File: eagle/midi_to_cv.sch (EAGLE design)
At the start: 75 parts, among them IC1 TL082P, IC2 TL084P, IC4 TL082P, IC6 TL082P, IC7 TL082P, U1 ATMEGA328P_PDIP, U2 MCP4822-E/P, U3 MCP4822-E/P, U4 MCP4822-E/P, U5 MCP4822-E/P

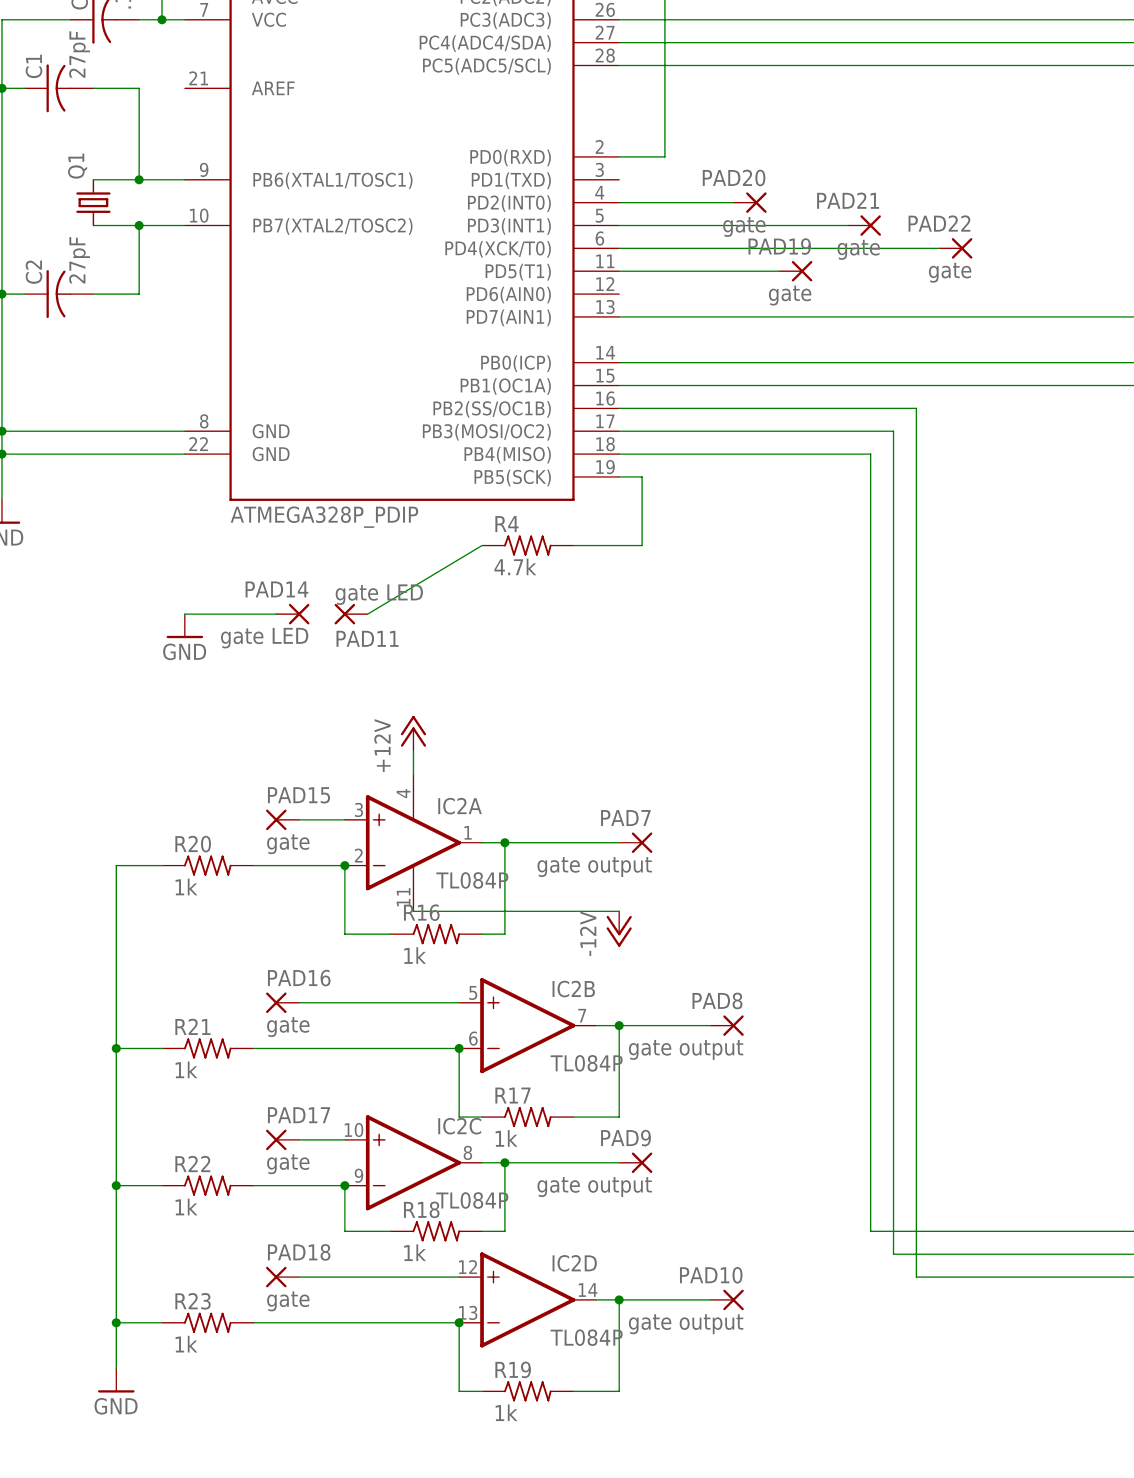
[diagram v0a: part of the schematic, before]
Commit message: will route gates to op amps instead of jumper pads
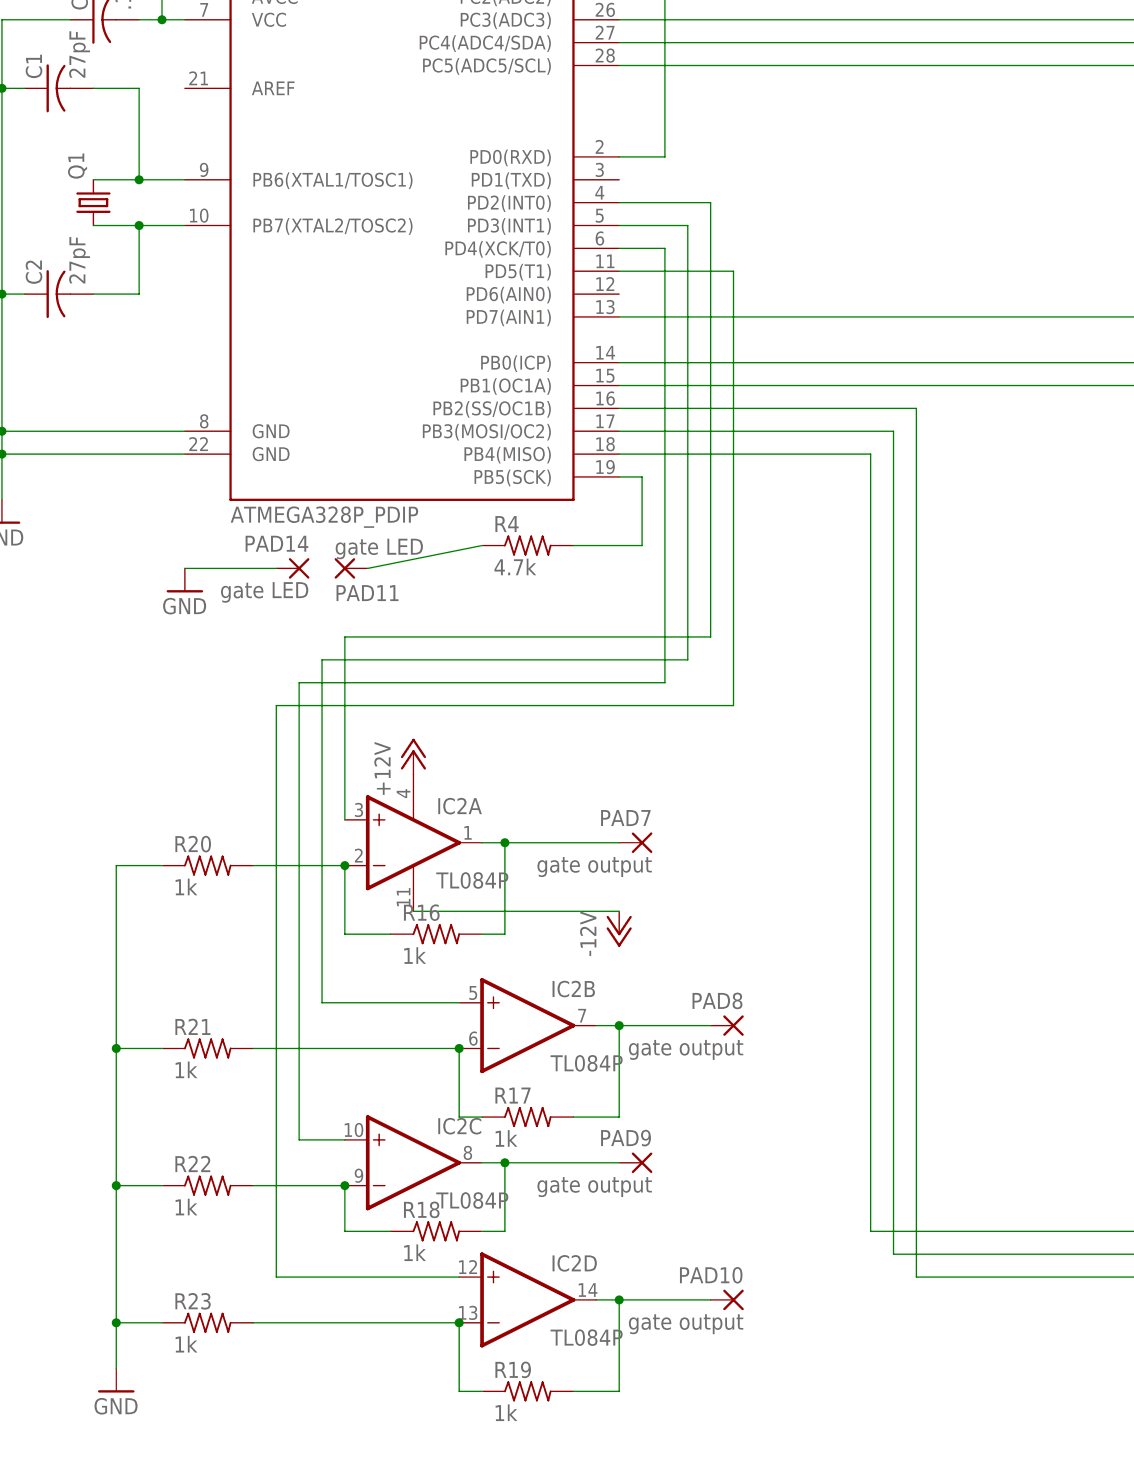
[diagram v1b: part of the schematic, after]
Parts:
- removed PAD15, PAD16, PAD17, PAD18, PAD19, PAD20, PAD21, PAD22: gate, wirepad:2,54/0,9
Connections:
- removed net N$31: PAD19.P, U1.PD5(T1)
- removed net N$32: PAD20.P, U1.PD2(INT0)
- removed net N$33: PAD21.P, U1.PD3(INT1)
- removed net N$43: PAD22.P, U1.PD4(XCK/T0)
- net N$34: now also U1.PD5(T1); no longer PAD18.P
- net N$44: now also U1.PD4(XCK/T0); no longer PAD17.P
- net N$45: now also U1.PD3(INT1); no longer PAD16.P
- net N$46: now also U1.PD2(INT0); no longer PAD15.P
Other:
- moved on the sheet: PAD11, PAD14
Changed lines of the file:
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@@
 <part name="P-2" library="supply1" deviceset="-12V" device=""/>
 <part name="P+8" library="supply1" deviceset="+12V" device=""/>
-<part name="PAD15" library="wirepad" deviceset="2,54/0,9" device="" value="gate"/>
-<part name="PAD16" library="wirepad" deviceset="2,54/0,9" device="" value="gate"/>
-<part name="PAD17" library="wirepad" deviceset="2,54/0,9" device="" value="gate"/>
-<part name="PAD18" library="wirepad" deviceset="2,54/0,9" device="" value="gate"/>
-<part name="PAD19" library="wirepad" deviceset="2,54/0,9" device="" value="gate"/>
-<part name="PAD20" library="wirepad" deviceset="2,54/0,9" device="" value="gate"/>
-<part name="PAD21" library="wirepad" deviceset="2,54/0,9" device="" value="gate"/>
-<part name="PAD22" library="wirepad" deviceset="2,54/0,9" device="" value="gate"/>
 <part name="GND5" library="supply1" deviceset="GND" device=""/>
 <part name="R8" library="rcl" deviceset="R-US_" device="0207/10" value="3.3k"/>
@@
 <instance part="IC2" gate="C" x="20.32" y="-60.96"/>
 <instance part="IC2" gate="D" x="33.02" y="-76.2"/>
-<instance part="PAD11" gate="1" x="12.7" y="0" rot="MR180"/>
+<instance part="PAD11" gate="1" x="12.7" y="5.08" rot="MR180"/>
 <instance part="R4" gate="G$1" x="33.02" y="7.62"/>
 <instance part="R16" gate="G$1" x="22.86" y="-35.56"/>
@@
 <instance part="PAD13" gate="1" x="10.16" y="83.82" rot="MR180"/>
 <instance part="GND9" gate="1" x="20.32" y="81.28"/>
-<instance part="PAD14" gate="1" x="7.62" y="0" rot="MR0"/>
-<instance part="GND11" gate="1" x="-5.08" y="-2.54"/>
+<instance part="PAD14" gate="1" x="7.62" y="5.08" rot="MR0"/>
+<instance part="GND11" gate="1" x="-5.08" y="2.54"/>
 <instance part="P-2" gate="1" x="43.18" y="-35.56"/>
-<instance part="P+8" gate="1" x="20.32" y="-12.7"/>
+<instance part="P+8" gate="1" x="20.32" y="-15.24"/>
 <instance part="IC2" gate="P" x="20.32" y="-25.4"/>
-<instance part="PAD15" gate="1" x="5.08" y="-22.86"/>
-<instance part="PAD16" gate="1" x="5.08" y="-43.18"/>
-<instance part="PAD17" gate="1" x="5.08" y="-58.42"/>
-<instance part="PAD18" gate="1" x="5.08" y="-73.66"/>
-<instance part="PAD19" gate="1" x="63.5" y="38.1" rot="MR0"/>
-<instance part="PAD20" gate="1" x="58.42" y="45.72" rot="MR0"/>
-<instance part="PAD21" gate="1" x="71.12" y="43.18" rot="MR0"/>
-<instance part="PAD22" gate="1" x="81.28" y="40.64" rot="MR0"/>
 <instance part="GND5" gate="1" x="109.22" y="-86.36"/>
 <instance part="R8" gate="G$1" x="177.8" y="124.46"/>
@@
 </segment>
 <segment>
-<wire x1="-5.08" y1="0" x2="5.08" y2="0" width="0.1524" layer="91"/>
+<wire x1="-5.08" y1="5.08" x2="5.08" y2="5.08" width="0.1524" layer="91"/>
 <pinref part="PAD14" gate="1" pin="P"/>
 <pinref part="GND11" gate="1" pin="GND"/>
@@
 <segment>
 <pinref part="P+8" gate="1" pin="+12V"/>
-<wire x1="20.32" y1="-17.78" x2="20.32" y2="-15.24" width="0.1524" layer="91"/>
 <pinref part="IC2" gate="P" pin="V+"/>
 </segment>
@@
 <pinref part="R4" gate="G$1" pin="1"/>
 <pinref part="PAD11" gate="1" pin="P"/>
-<wire x1="27.94" y1="7.62" x2="15.24" y2="0" width="0.1524" layer="91"/>
-</segment>
-</net>
-<net name="N$32" class="0">
-<segment>
-<pinref part="U1" gate="G$1" pin="PD2(INT0)"/>
-<wire x1="43.18" y1="45.72" x2="55.88" y2="45.72" width="0.1524" layer="91"/>
-<pinref part="PAD20" gate="1" pin="P"/>
-</segment>
-</net>
-<net name="N$33" class="0">
-<segment>
-<pinref part="U1" gate="G$1" pin="PD3(INT1)"/>
-<wire x1="43.18" y1="43.18" x2="68.58" y2="43.18" width="0.1524" layer="91"/>
-<pinref part="PAD21" gate="1" pin="P"/>
+<wire x1="27.94" y1="7.62" x2="15.24" y2="5.08" width="0.1524" layer="91"/>
 </segment>
 </net>
@@
 <segment>
 <pinref part="IC2" gate="D" pin="+IN"/>
-<wire x1="7.62" y1="-73.66" x2="25.4" y2="-73.66" width="0.1524" layer="91"/>
-<pinref part="PAD18" gate="1" pin="P"/>
+<wire x1="5.08" y1="-73.66" x2="25.4" y2="-73.66" width="0.1524" layer="91"/>
+<wire x1="5.08" y1="-73.66" x2="5.08" y2="-10.16" width="0.1524" layer="91"/>
+<wire x1="5.08" y1="-10.16" x2="55.88" y2="-10.16" width="0.1524" layer="91"/>
+<wire x1="55.88" y1="-10.16" x2="55.88" y2="38.1" width="0.1524" layer="91"/>
+<pinref part="U1" gate="G$1" pin="PD5(T1)"/>
+<wire x1="55.88" y1="38.1" x2="43.18" y2="38.1" width="0.1524" layer="91"/>
 </segment>
 </net>
@@
 </segment>
 </net>
-<net name="N$43" class="0">
-<segment>
-<pinref part="U1" gate="G$1" pin="PD4(XCK/T0)"/>
-<wire x1="43.18" y1="40.64" x2="78.74" y2="40.64" width="0.1524" layer="91"/>
-<pinref part="PAD22" gate="1" pin="P"/>
-</segment>
-</net>
 <net name="N$44" class="0">
 <segment>
 <pinref part="IC2" gate="C" pin="+IN"/>
 <wire x1="7.62" y1="-58.42" x2="12.7" y2="-58.42" width="0.1524" layer="91"/>
-<pinref part="PAD17" gate="1" pin="P"/>
+<pinref part="U1" gate="G$1" pin="PD4(XCK/T0)"/>
+<wire x1="43.18" y1="40.64" x2="48.26" y2="40.64" width="0.1524" layer="91"/>
+<wire x1="48.26" y1="40.64" x2="48.26" y2="-7.62" width="0.1524" layer="91"/>
+<wire x1="48.26" y1="-7.62" x2="7.62" y2="-7.62" width="0.1524" layer="91"/>
+<wire x1="7.62" y1="-7.62" x2="7.62" y2="-58.42" width="0.1524" layer="91"/>
 </segment>
 </net>
@@
 <segment>
 <pinref part="IC2" gate="B" pin="+IN"/>
-<wire x1="7.62" y1="-43.18" x2="25.4" y2="-43.18" width="0.1524" layer="91"/>
-<pinref part="PAD16" gate="1" pin="P"/>
+<pinref part="U1" gate="G$1" pin="PD3(INT1)"/>
+<wire x1="10.16" y1="-43.18" x2="25.4" y2="-43.18" width="0.1524" layer="91"/>
+<wire x1="43.18" y1="43.18" x2="50.8" y2="43.18" width="0.1524" layer="91"/>
+<wire x1="50.8" y1="43.18" x2="50.8" y2="-5.08" width="0.1524" layer="91"/>
+<wire x1="50.8" y1="-5.08" x2="10.16" y2="-5.08" width="0.1524" layer="91"/>
+<wire x1="10.16" y1="-5.08" x2="10.16" y2="-43.18" width="0.1524" layer="91"/>
 </segment>
 </net>
 <net name="N$46" class="0">
 <segment>
-<pinref part="PAD15" gate="1" pin="P"/>
 <pinref part="IC2" gate="A" pin="+IN"/>
-<wire x1="7.62" y1="-22.86" x2="12.7" y2="-22.86" width="0.1524" layer="91"/>
+<pinref part="U1" gate="G$1" pin="PD2(INT0)"/>
+<wire x1="43.18" y1="45.72" x2="53.34" y2="45.72" width="0.1524" layer="91"/>
+<wire x1="53.34" y1="45.72" x2="53.34" y2="-2.54" width="0.1524" layer="91"/>
+<wire x1="53.34" y1="-2.54" x2="12.7" y2="-2.54" width="0.1524" layer="91"/>
+<wire x1="12.7" y1="-2.54" x2="12.7" y2="-22.86" width="0.1524" layer="91"/>
 </segment>
 </net>
@@
 </segment>
 </net>
-<net name="N$31" class="0">
-<segment>
-<pinref part="U1" gate="G$1" pin="PD5(T1)"/>
-<pinref part="PAD19" gate="1" pin="P"/>
-<wire x1="43.18" y1="38.1" x2="60.96" y2="38.1" width="0.1524" layer="91"/>
-</segment>
-</net>
